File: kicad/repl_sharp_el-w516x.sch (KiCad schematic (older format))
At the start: 140 parts, among them J1 USB_B_Micro, SW1 SW_Push, SW10 SW_Push, SW11 SW_Push, SW12 SW_Push, SW13 SW_Push, SW14 SW_Push, SW15 SW_Push, SW16 SW_Push, SW17 SW_Push, SW18 SW_Push, SW19 SW_Push, SW2 SW_Push, SW20 SW_Push, SW21 SW_Push, SW22 SW_Push, SW23 SW_Push, SW24 SW_Push, SW25 SW_Push, SW26 SW_Push, SW27 SW_Push, SW28 SW_Push, SW29 SW_Push, SW3 SW_Push, SW30 SW_Push, SW31 SW_Push, SW32 SW_Push, SW33 SW_Push, SW34 SW_Push, SW35 SW_Push, SW36 SW_Push, SW37 SW_Push, SW38 SW_Push, SW39 SW_Push, SW4 SW_Push, SW40 SW_Push, SW41 SW_Push, SW42 SW_Push, SW43 SW_Push, SW44 SW_Push, SW45 SW_Push, SW46 SW_Push, SW47 SW_Push, SW48 SW_Push, SW49 SW_Push, SW5 SW_Push, SW50 SW_Push, SW51 SW_Push, SW52 SW_Push, SW53 SW_Push, SW54 SW_Push, SW55 SW_Push, SW56 SW_Push, SW57 SW_Push, SW6 SW_Push, SW7 SW_Push, SW8 SW_Push, SW9 SW_Push, U1 74HC165D, U2 ATmega32U4-AU, U3 74HC595, Y1 Crystal

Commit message: kicad: update schematic and pcb
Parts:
- removed C1, C3, C5, C6: 0.1u, symbol Device:C_Small
- removed C7: 4.7u, symbol Device:C_Small
- removed D1, D10, D11, D12, D13, D14, D15, D16, D17, D18, D19, D2, D20, D21, D22, D23, D24, D25, D26, D27, D28, D29, D3, D30, D31, D32, D33, D34, D35, D36, D37, D38, D39, D4, D40, D41, D42, D43, D44, D45, D46, D47, D48, D49, D5, D50, D51, D52, D53, D54, D55, D56, D6, D7, D8, D9: D, symbol Device:D
- removed R10, R11, R12, R4, R6, R7, R8, R9: 10k, symbol Device:R
- removed SW10, SW11, SW12, SW13, SW14, SW15, SW16, SW17, SW18, SW19, SW2, SW20, SW21, SW22, SW23, SW24, SW25, SW26, SW27, SW28, SW29, SW3, SW30, SW31, SW32, SW33, SW34, SW35, SW36, SW37, SW38, SW39, SW4, SW40, SW41, SW42, SW43, SW44, SW45, SW46, SW47, SW48, SW49, SW5, SW50, SW51, SW52, SW53, SW54, SW55, SW56, SW57, SW6, SW7, SW8, SW9: SW_Push, symbol Switch:SW_Push
- added C12: 4.7u, Capacitor_SMD:C_0603_1608Metric_Pad1.05x0.95mm_HandSolder, symbol Device:C_Small
- added C14, C15, C17, C18, C19: 0.1u, Capacitor_SMD:C_0603_1608Metric_Pad1.05x0.95mm_HandSolder, symbol Device:C_Small
- added C16, C20, C21: 1u, Capacitor_SMD:C_0603_1608Metric_Pad1.05x0.95mm_HandSolder, symbol Device:C_Small
- added DS1: NHD-C12832A1Z-FSW-FBW-3V3, NHD-C12832A1Z-FSW-FBW-3V3:NHDC12832A1ZFSWFBW3V3, symbol NHD-C12832A1Z-FSW-FBW-3V3:NHD-C12832A1Z-FSW-FBW-3V3
- added J3: AVR-ISP-6, Connector_PinHeader_1.27mm:PinHeader_2x03_P1.27mm_Vertical_SMD, symbol Connector:AVR-ISP-6
- C10, C2, C4, C8, C9: footprint (none) -> Capacitor_SMD:C_0603_1608Metric_Pad1.05x0.95mm_HandSolder
- J1: footprint (none) -> Connector_USB:USB_Micro-B_Amphenol_10103594-0001LF_Horizontal
- R1, R2, R3, R5: footprint (none) -> Resistor_SMD:R_0603_1608Metric_Pad1.05x0.95mm_HandSolder
- SW1: value SW_Push -> SW_RESET; footprint (none) -> Button_Switch_SMD:SW_Push_1P1T_NO_6x6mm_H9.5mm
- U1: footprint SOT109-1 -> footprints:74HC165D
- U3: footprint (none) -> Package_SO:SOIC-16_3.9x9.9mm_P1.27mm
- Y1: footprint (none) -> Crystal:Crystal_SMD_5032-2Pin_5.0x3.2mm
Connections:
- net GND: now also SW1.1, U3.13 (~OE), C12.1, C14.1, C15.1, C16.1, C17.1, C18.1, C19.1, DS1.11 (VSS), DS1.17 (CS1B), DS1.MH2, J3.6 (GND); no longer R1.2, U3.14 (SER)
- net shift_out_n_srclr: now reaches U2.25 (PD4), U3.10 (~SRCLR)
- net shift_out_srclk: now reaches U2.28 (PB4), U3.11 (SRCLK)
- net shift_out_rclk: now reaches U2.26 (PD6), U3.12 (RCLK)
- net shift_in_pl: now reaches U2.27 (PD7)
- net shift_in_pl: now also U1.1 (PL*); no longer U3.13 (~OE)
- net lcd_mosi: now reaches U2.10 (PB2)
- net lcd_mosi: now also DS1.13 (SI), J3.4 (MOSI)
- net uc_miso: now reaches U2.11 (PB3)
- net uc_miso: now also J3.1 (MISO)
- net lcd_n_res: now reaches U2.12 (PB7)
- net lcd_n_res: now also DS1.16 (/RES)
- net uc_n_reset: now reaches R1.1, SW1.2, U2.13 (~RESET)
- net uc_n_reset: now also J3.5 (~RST)
- net lcd_reg_sel: now reaches U2.29 (PB5)
- net lcd_reg_sel: now also DS1.15 (A0)
- net shift_out_ser: now reaches U2.32 (PC7)
- net shift_out_ser: now also U3.14 (SER)
- net lcd_scl: now reaches U2.9 (PB1)
- net lcd_scl: now also DS1.14 (SCK), J3.3 (SCK)
- net D-: now reaches J1.2 (D-), R3.2
- net D+: now reaches J1.3 (D+), R2.2
- net VCC renamed +3V3
- net +3V3: now also R1.2, DS1.12 (VDD), DS1.MH1, J3.2 (VCC); no longer J1.1 (VBUS), SW1.1, U1.1 (PL*), U2.2 (UVCC), U2.7 (VBUS)
- new net: C17.2, DS1.1 (V0)
- new net: C16.2, DS1.10 (VOUT)
- new net: C14.2, DS1.2 (V1)
- new net: C18.2, DS1.3 (V2)
- new net: C15.2, DS1.4 (V3)
- new net: C19.2, DS1.5 (V4)
- new net: C20.1, DS1.6 (C2-)
- new net: C20.2, DS1.7 (C2+)
- new net: C21.1, DS1.8 (C1+)
- new net: C21.2, DS1.9 (C1-)
- new net VBUS: C12.2, J1.1 (VBUS), U2.2 (UVCC), U2.7 (VBUS)
- no-connect marks 24 -> 17
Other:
- note added: "REPLACE WITH UC CONTROL"
- moved on the sheet: C10, C2, C4, C8, C9, J1, R1, R2, R3, R5, SW1, U1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

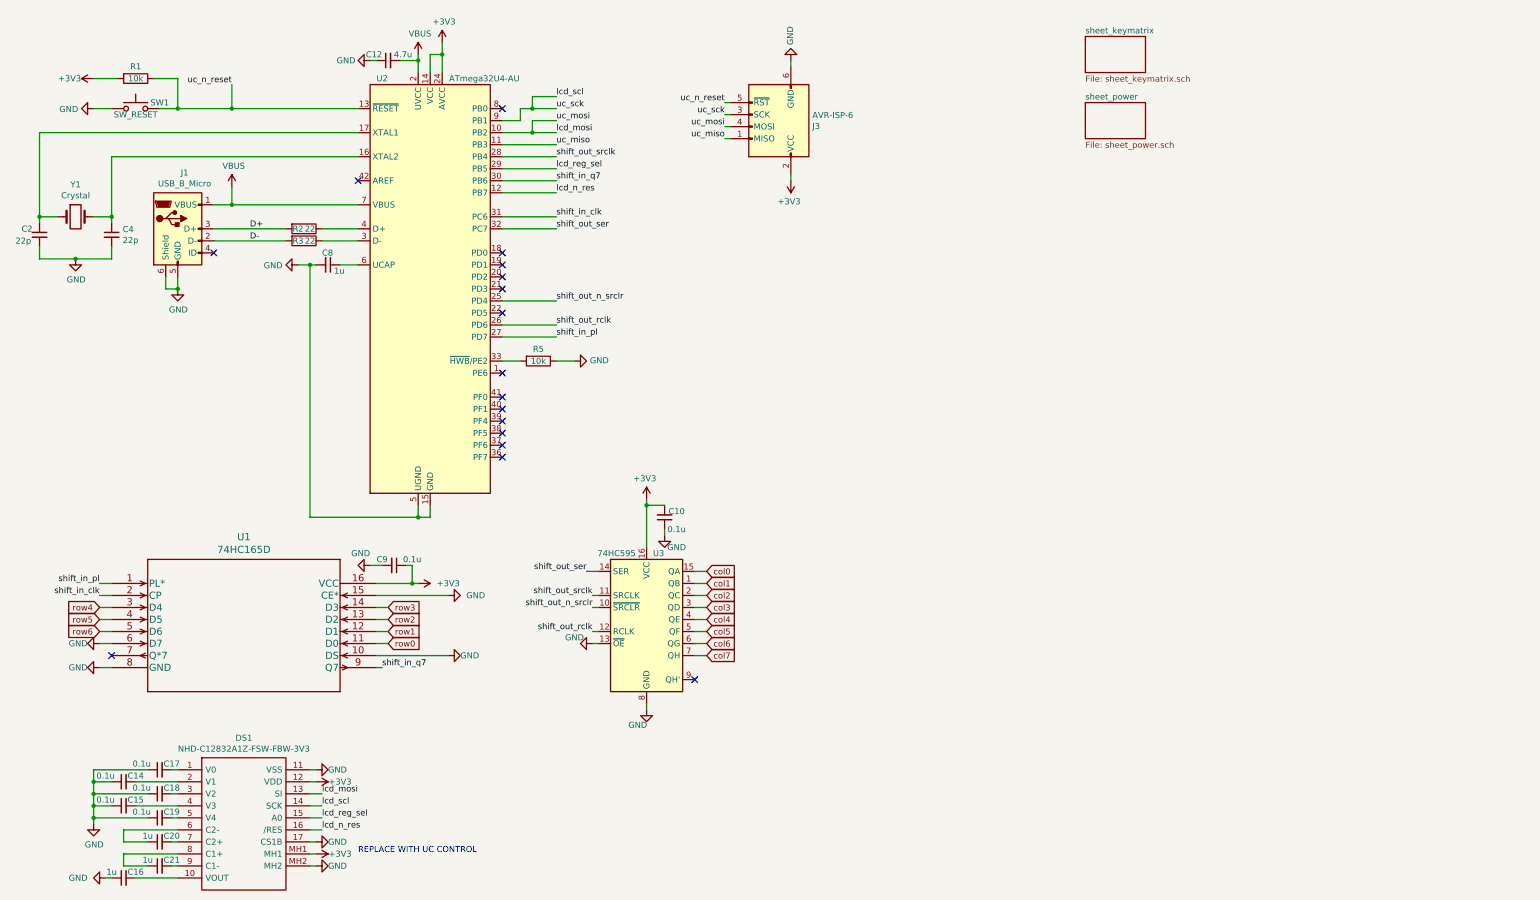
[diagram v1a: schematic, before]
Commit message: kicad: completed partial layout
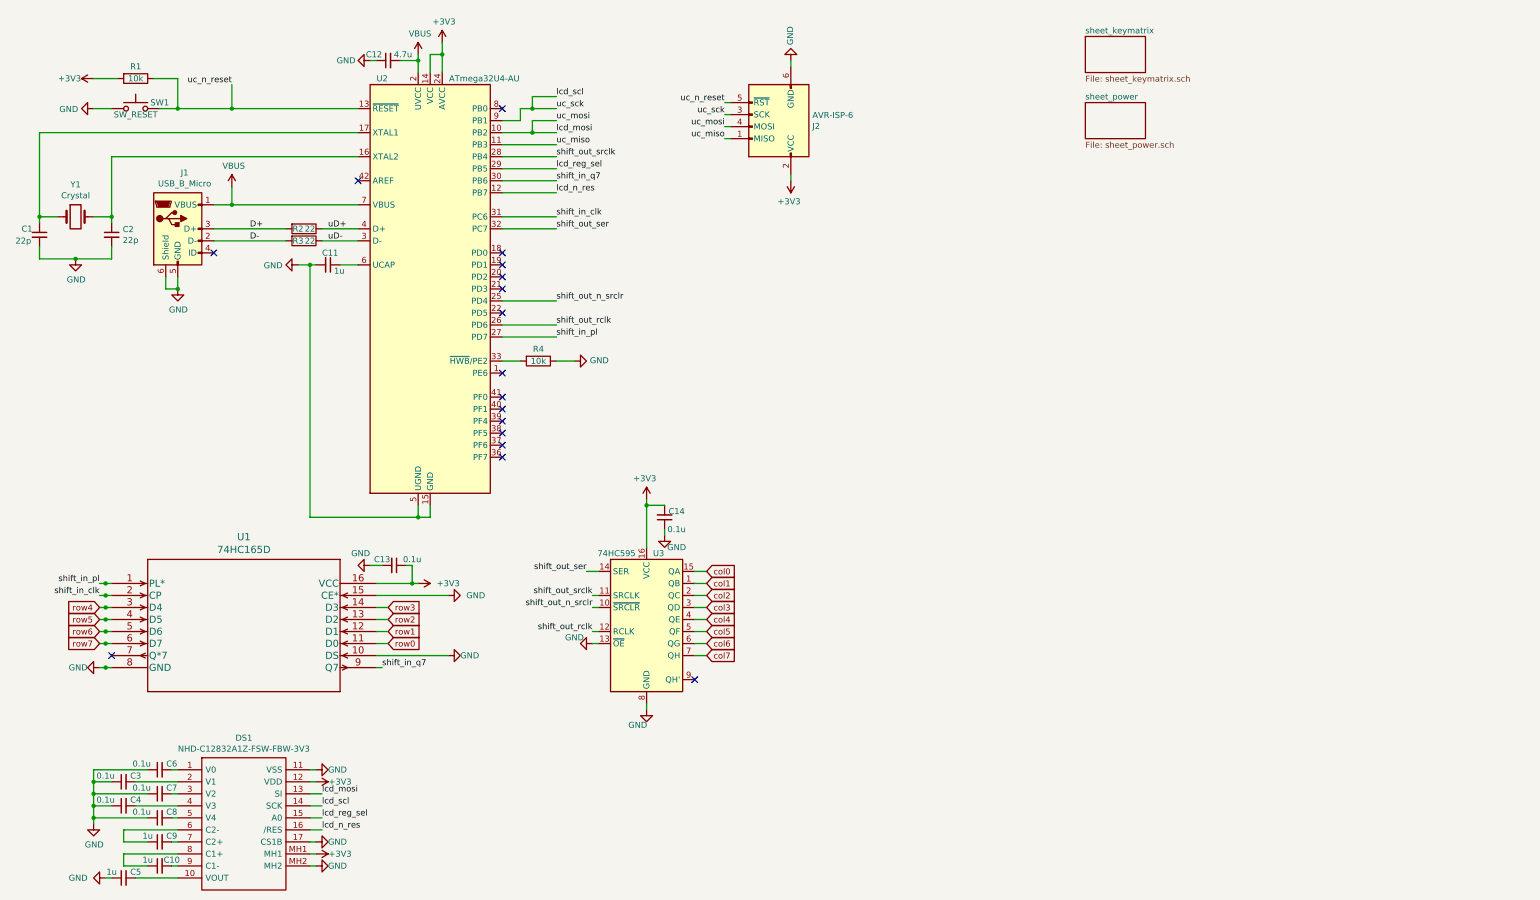
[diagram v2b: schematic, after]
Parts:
- renumbered C2 to C1, C21 to C10, C8 to C11, C9 to C13, C10 to C14, C4 to C2, C14 to C3, C15 to C4, C16 to C5, C17 to C6, C18 to C7, C19 to C8, C20 to C9, J3 to J2, R5 to R4
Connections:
- net GND: no longer U1.6 (D7)
- net uD-: now reaches R3.1, U2.3 (D-)
- net uD+: now reaches R2.1, U2.4 (D+)
- new net row7: U1.6 (D7)
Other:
- note removed: "REPLACE WITH UC CONTROL"

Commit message: kicad: finalize design
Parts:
- added D11: LED, Diode_SMD:D_0603_1608Metric_Pad1.05x0.95mm_HandSolder, symbol Device:LED
- added R18: 1k, Resistor_SMD:R_0603_1608Metric_Pad1.05x0.95mm_HandSolder, symbol Device:R
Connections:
- net GND: now also R18.2
- net at U2.18 (PD0): now also D11.2 (A)
- new net: D11.1 (K), R18.1
- no-connect marks 17 -> 16
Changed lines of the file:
@@
 $EndComp
-Wire Wire Line
-	1250 5500 1300 5500
-Wire Wire Line
-	1250 5600 1300 5600
-Wire Wire Line
-	1250 5700 1300 5700
 Wire Wire Line
 	3550 5500 3650 5500
@@
 Wire Wire Line
 	3850 5300 3550 5300
-Wire Wire Line
-	1350 5800 1300 5800
 $Comp
 L power:GND #PWR05
@@
 	0    1    1    0
 $EndComp
-Wire Wire Line
-	1250 6000 1300 6000
 Wire Wire Line
 	3500 5150 3600 5150
@@
 Text Label 1250 5400 2    50   ~ 0
 shift_in_clk
-Wire Wire Line
-	1250 5400 1300 5400
 $Comp
 L Device:C_Small C6
@@
 Text Label 1250 5300 2    50   ~ 0
 shift_in_pl
-Wire Wire Line
-	1250 5300 1300 5300
 Text Label 5350 5500 2    50   ~ 0
 shift_out_n_srclr
@@
 	3900 900  3900 950
 NoConn ~ 4600 2650
-NoConn ~ 4600 2550
 Wire Wire Line
 	750  1550 3400 1550
@@
 Wire Wire Line
 	5050 2350 4600 2350
-$Comp
-L MCU_Microchip_ATmega:ATmega32U4-AU U2
-U 1 1 5CF843C0
-P 4000 2850
-F 0 "U2" H 3600 4600 50  0000 C CNN
-F 1 "ATmega32U4-AU" H 4450 4600 50  0000 C CNN
-F 2 "Package_QFP:TQFP-44_10x10mm_P0.8mm" H 4000 2850 50  0001 C CIN
-F 3 "http://ww1.microchip.com/downloads/en/DeviceDoc/Atmel-7766-8-bit-AVR-ATmega16U4-32U4_Datasheet.pdf" H 4000 2850 50  0001 C CNN
-	1    4000 2850
-	1    0    0    -1
-$EndComp
 Text Label 5050 1250 0    50   ~ 0
 lcd_scl
@@
 Text Label 3150 2450 0    50   ~ 0
 uD-
-Connection ~ 1300 5300
-Wire Wire Line
-	1300 5300 1350 5300
-Connection ~ 1300 5400
-Wire Wire Line
-	1300 5400 1350 5400
-Connection ~ 1300 5500
-Wire Wire Line
-	1300 5500 1350 5500
-Connection ~ 1300 5600
-Wire Wire Line
-	1300 5600 1350 5600
-Connection ~ 1300 5700
-Wire Wire Line
-	1300 5700 1350 5700
-Connection ~ 1300 5800
-Wire Wire Line
-	1300 5800 1250 5800
-Connection ~ 1300 6000
-Wire Wire Line
-	1300 6000 1350 6000
 $Comp
 L 74HC165D:74HC165D U1
@@
 Text GLabel 1250 5800 0    50   Input ~ 0
 row7
+Wire Wire Line
+	1250 5500 1350 5500
+Wire Wire Line
+	1250 5600 1350 5600
+Wire Wire Line
+	1250 5700 1350 5700
+Wire Wire Line
+	1250 5800 1350 5800
+Wire Wire Line
+	1250 6000 1350 6000
+Wire Wire Line
+	1250 5400 1350 5400
+Wire Wire Line
+	1250 5300 1350 5300
+$Comp
+L MCU_Microchip_ATmega:ATmega32U4-AU U2
+U 1 1 5CF843C0
+P 4000 2850
+F 0 "U2" H 3600 4600 50  0000 C CNN
+F 1 "ATmega32U4-AU" H 4450 4600 50  0000 C CNN
+F 2 "Package_QFP:TQFP-44_10x10mm_P0.8mm" H 4000 2850 50  0001 C CIN
+F 3 "http://ww1.microchip.com/downloads/en/DeviceDoc/Atmel-7766-8-bit-AVR-ATmega16U4-32U4_Datasheet.pdf" H 4000 2850 50  0001 C CNN
+	1    4000 2850
+	1    0    0    -1
+$EndComp
+$Comp
+L Device:LED D11
+U 1 1 5D2BBCCA
+P 4850 2550
+F 0 "D11" H 4850 2450 50  0000 C CNN
+F 1 "LED" H 4850 2650 50  0000 C CNN
+F 2 "Diode_SMD:D_0603_1608Metric_Pad1.05x0.95mm_HandSolder" H 4850 2550 50  0001 C CNN
+F 3 "~" H 4850 2550 50  0001 C CNN
+	1    4850 2550
+	-1   0    0    1
+$EndComp
+Wire Wire Line
+	4600 2550 4700 2550
+$Comp
+L Device:R R?
+U 1 1 5D2D5095
+P 5200 2550
+AR Path="/6129FE6A/5D2D5095" Ref="R?"  Part="1"
+AR Path="/5D2D5095" Ref="R18"  Part="1"
+F 0 "R18" V 5300 2550 50  0000 C CNN
+F 1 "1k" V 5200 2550 50  0000 C CNN
+F 2 "Resistor_SMD:R_0603_1608Metric_Pad1.05x0.95mm_HandSolder" V 5130 2550 50  0001 C CNN
+F 3 "~" H 5200 2550 50  0001 C CNN
+	1    5200 2550
+	0    -1   1    0
+$EndComp
+Wire Wire Line
+	5050 2550 5000 2550
+$Comp
+L power:GND #PWR048
+U 1 1 5D2E4394
+P 5400 2550
+F 0 "#PWR048" H 5400 2300 50  0001 C CNN
+F 1 "GND" V 5405 2422 50  0000 R CNN
+F 2 "" H 5400 2550 50  0001 C CNN
+F 3 "" H 5400 2550 50  0001 C CNN
+	1    5400 2550
+	0    -1   -1   0
+$EndComp
+Wire Wire Line
+	5400 2550 5350 2550
 $EndSCHEMATC

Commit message: kicad: design after production
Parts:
- added JP1: Jumper_2_Open, Jumper:SolderJumper-2_P1.3mm_Open_Pad1.0x1.5mm, symbol Jumper:Jumper_2_Open
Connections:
- net +3V3: now also R4.1
- net GND: now also JP1.2 (B); no longer R4.1
- net at R4.2, U2.33 (~HWB~/PE2): now also JP1.1 (A)
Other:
- moved on the sheet: R4
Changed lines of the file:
@@
 L Device:R R4
 U 1 1 5D0087A6
-P 4900 3450
-F 0 "R4" V 4800 3450 50  0000 C CNN
-F 1 "10k" V 4900 3450 50  0000 C CNN
-F 2 "Resistor_SMD:R_0603_1608Metric_Pad1.05x0.95mm_HandSolder" V 4830 3450 50  0001 C CNN
-F 3 "~" H 4900 3450 50  0001 C CNN
-	1    4900 3450
+P 5500 3450
+F 0 "R4" V 5400 3450 50  0000 C CNN
+F 1 "10k" V 5500 3450 50  0000 C CNN
+F 2 "Resistor_SMD:R_0603_1608Metric_Pad1.05x0.95mm_HandSolder" V 5430 3450 50  0001 C CNN
+F 3 "~" H 5500 3450 50  0001 C CNN
+	1    5500 3450
 	0    1    1    0
 $EndComp
@@
 P 1550 1350
 F 0 "SW1" H 1750 1400 50  0000 C CNN
-F 1 "SW_RESET" H 1550 1300 50  0000 C CNN
+F 1 "SW_RESET" H 1550 1250 50  0000 C CNN
 F 2 "Button_Switch_SMD:SW_Push_1P1T_NO_6x6mm_H9.5mm" H 1550 1550 50  0001 C CNN
 F 3 "~" H 1550 1550 50  0001 C CNN
@@
 U 1 1 5CF8C1A5
 P 750 2400
-F 0 "C1" H 600 2450 50  0000 L CNN
-F 1 "22p" H 550 2350 50  0000 L CNN
+F 0 "C1" H 550 2450 50  0000 L CNN
+F 1 "22p" H 500 2350 50  0000 L CNN
 F 2 "Capacitor_SMD:C_0603_1608Metric_Pad1.05x0.95mm_HandSolder" H 750 2400 50  0001 C CNN
 F 3 "~" H 750 2400 50  0001 C CNN
@@
 P 5350 5800
 F 0 "#PWR023" H 5350 5550 50  0001 C CNN
-F 1 "GND" V 5300 5650 50  0000 C CNN
+F 1 "GND" V 5350 5600 50  0000 C CNN
 F 2 "" H 5350 5800 50  0001 C CNN
 F 3 "" H 5350 5800 50  0001 C CNN
@@
 NoConn ~ 4600 4150
 NoConn ~ 4600 4250
-Wire Wire Line
-	4600 3450 4750 3450
 Wire Wire Line
 	3400 2450 3100 2450
@@
 shift_in_q7
 Wire Wire Line
-	5050 3450 5200 3450
+	5650 3450 5800 3450
 $Comp
 L power:GND #PWR022
 U 1 1 5D008D49
-P 5200 3450
-F 0 "#PWR022" H 5200 3200 50  0001 C CNN
-F 1 "GND" V 5205 3322 50  0000 R CNN
-F 2 "" H 5200 3450 50  0001 C CNN
-F 3 "" H 5200 3450 50  0001 C CNN
-	1    5200 3450
+P 5800 3650
+F 0 "#PWR022" H 5800 3400 50  0001 C CNN
+F 1 "GND" V 5805 3522 50  0000 R CNN
+F 2 "" H 5800 3650 50  0001 C CNN
+F 3 "" H 5800 3650 50  0001 C CNN
+	1    5800 3650
 	0    -1   -1   0
 $EndComp
@@
 Wire Wire Line
 	5400 2550 5350 2550
+$Comp
+L Jumper:Jumper_2_Open JP1
+U 1 1 5D2BC128
+P 5050 3650
+F 0 "JP1" H 5050 3450 50  0000 C CNN
+F 1 "Jumper_2_Open" H 5050 3550 50  0000 C CNN
+F 2 "Jumper:SolderJumper-2_P1.3mm_Open_Pad1.0x1.5mm" H 5050 3650 50  0001 C CNN
+F 3 "~" H 5050 3650 50  0001 C CNN
+	1    5050 3650
+	1    0    0    -1
+$EndComp
+Wire Wire Line
+	4600 3450 4850 3450
+$Comp
+L power:+3V3 #PWR0101
+U 1 1 5D2D9C91
+P 5800 3450
+F 0 "#PWR0101" H 5800 3300 50  0001 C CNN
+F 1 "+3V3" H 5815 3623 50  0000 C CNN
+F 2 "" H 5800 3450 50  0001 C CNN
+F 3 "" H 5800 3450 50  0001 C CNN
+	1    5800 3450
+	0    1    1    0
+$EndComp
+Wire Wire Line
+	4850 3650 4850 3450
+Connection ~ 4850 3450
+Wire Wire Line
+	4850 3450 5350 3450
+Wire Wire Line
+	5800 3650 5250 3650
 $EndSCHEMATC

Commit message: kicad: finalize device BOM
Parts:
- C1, C2: Description (none) -> Oscillator load; Digi-Key PN (none) -> 311-1062-1-ND; Digi-Key Page (none) -> https://www.digikey.com/product-detail/en/yageo/CC0603JRNPO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
- C10, C11, C5, C9: Description (none) -> Assorted decoupling; Digi-Key PN (none) -> 1276-1182-1-ND; Digi-Key Page (none) -> https://www.digikey.com/product-detail/en/samsung-electro-m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
- C12: Description (none) -> USB power decoupling; Digi-Key PN (none) -> 1276-1045-1-ND; Digi-Key Page (none) -> https://www.digikey.com/product-detail/en/samsung-electro-m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
- C13, C14, C3, C4, C6, C7, C8: Description (none) -> Assorted display; Digi-Key PN (none) -> 1276-1005-1-ND; Digi-Key Page (none) -> https://www.digikey.com/product-detail/en/samsung-electro-m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
- D11: Description (none) -> Indicator LED; Digi-Key PN (none) -> SML-D12U1WT86CT-ND; Digi-Key Page (none) -> https://www.digikey.com/product-detail/en/rohm-semiconducto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
- DS1: Digi-Key PN (none) -> NHD-C12832A1Z-FSW-FBW-3V3-ND; Digi-Key Page (none) -> https://www.digikey.com/product-detail/en/newhaven-display-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
- J1: Description (none) -> USB Micro B Amphenol; Digi-Key PN (none) -> 609-4613-1-ND; Digi-Key Page (none) -> https://www.digikey.com/product-detail/en/amphenol-icc-fci/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
- R1, R4: Description (none) -> Input pull-down resistor; Digi-Key PN (none) -> 311-10.0KHRCT-ND; Digi-Key Page (none) -> https://www.digikey.com/product-detail/en/yageo/RC0603FR-07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
- R18: Description (none) -> LED current limiting; Digi-Key PN (none) -> 311-1.00KHRCT-ND; Digi-Key Page (none) -> https://www.digikey.com/product-detail/en/yageo/RC0603FR-07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
- R2, R3: Description (none) -> USB data resistor; Digi-Key PN (none) -> 311-22.0HRCT-ND; Digi-Key Page (none) -> https://www.digikey.com/product-detail/en/yageo/RC0603FR-07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
- SW1: Description (none) -> Reset button; Digi-Key PN (none) -> CKN9112CT-ND; Digi-Key Page (none) -> https://www.digikey.com/product-detail/en/c-k/PTS645SM43SMT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
- U1: footprint footprints:74HC165D -> Package_SO:SOIC-16_3.9x9.9mm_P1.27mm; Description (none) -> 8-bit PISO Shift Register; Digi-Key PN (none) -> 1727-3782-ND; Digi-Key Page (none) -> https://www.digikey.com/product-detail/en/nexperia-usa-inc/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
- U2: Description (none) -> ATMEGA32U4-AU uC; Digi-Key PN (none) -> ATMEGA32U4-AURCT-ND; Digi-Key Page (none) -> https://www.digikey.com/product-detail/en/microchip-technol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
- U3: Description (none) -> 8-bit SIPO Shift Register; Digi-Key PN (none) -> 296-14857-1-ND; Digi-Key Page (none) -> https://www.digikey.com/product-detail/en/texas-instruments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
- Y1: Description (none) -> 8MHz ±20ppm Crystal 18pF 100 Ohms 2-SMD; Digi-Key PN (none) -> XC2103CT-ND; Digi-Key Page (none) -> https://www.digikey.com/product-detail/en/ecs-inc/ECS-80-18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
